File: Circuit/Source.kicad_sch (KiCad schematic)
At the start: 42 parts, among them K1 AGQ200A12, Q1 2N7002, Q2 TIP41C, Q3 TIP42C, U2 DG201, U3 OPA2197xD, U4 OPA2197xD, U5 OPA2197xD

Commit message: Output job, Revision Box and reorganise
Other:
- company: Harry and Yuki - EEE3 Instrumentation -> Harry Hill and Yuki Hoshino
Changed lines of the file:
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@@
 	(title_block
 		(title "Signal Source")
-		(date "2026-03-02")
+		(date "2026-05-02")
 		(rev "1.0")
-		(company "Harry and Yuki - EEE3 Instrumentation")
+		(company "Harry Hill and Yuki Hoshino")
+		(comment 1 "LCR Meter")
 	)
 	(text "Bias range:\n±10V\nGain:\n~6.5"

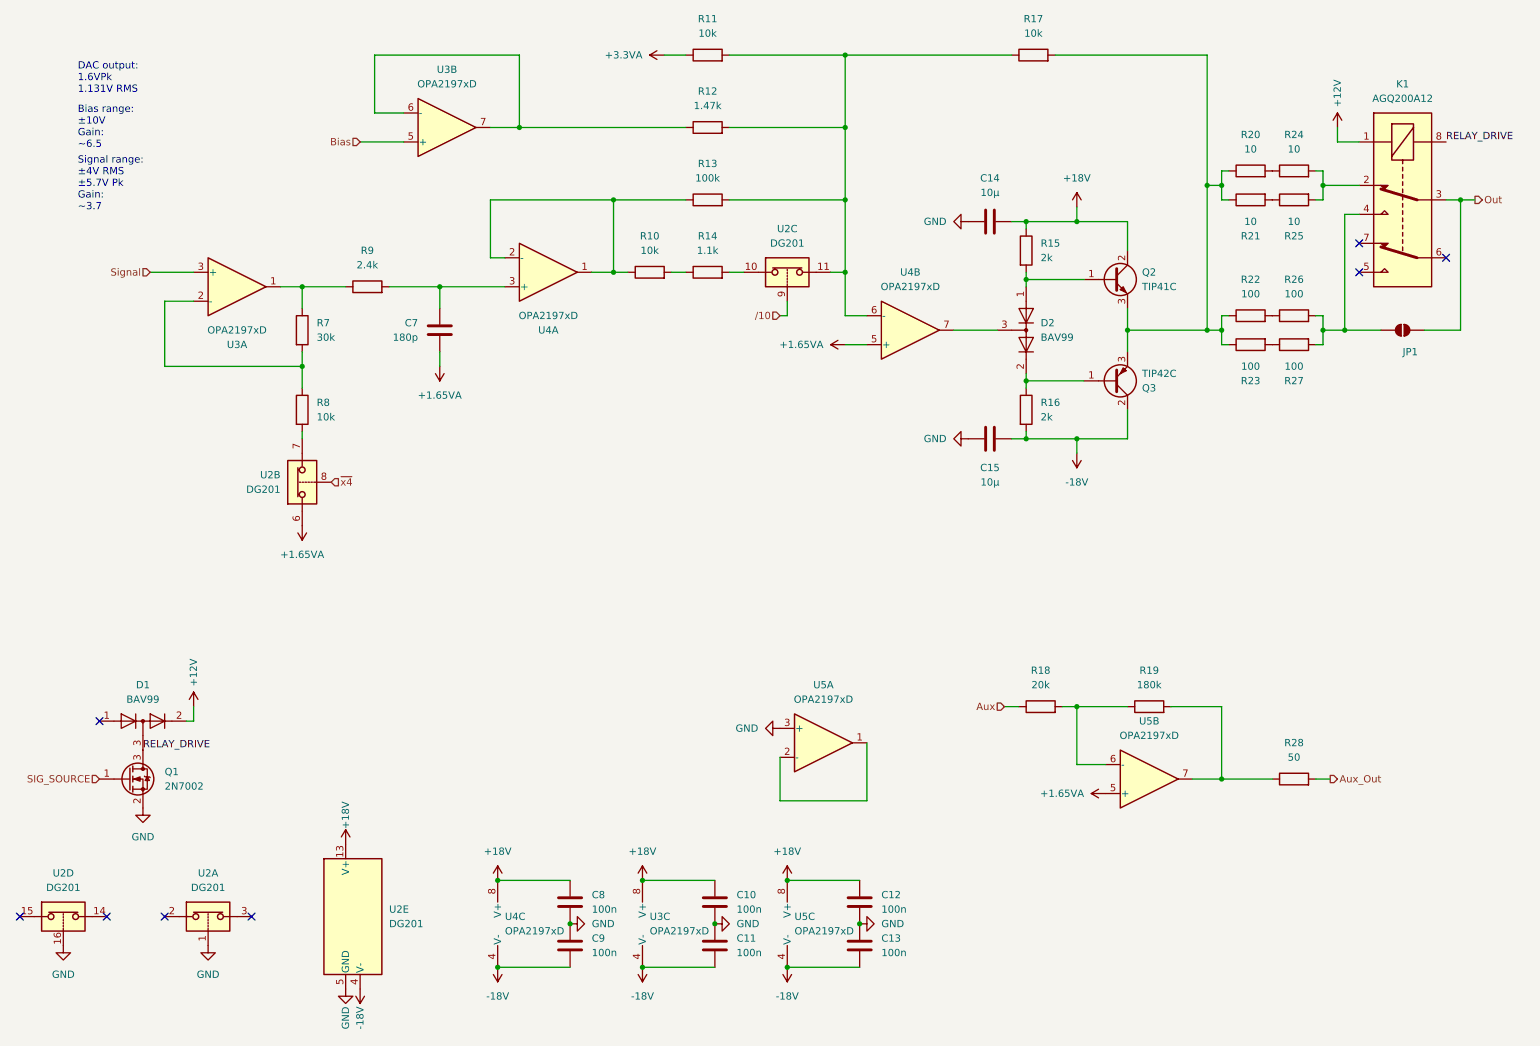
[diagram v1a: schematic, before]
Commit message: Input Protection Second Attempt
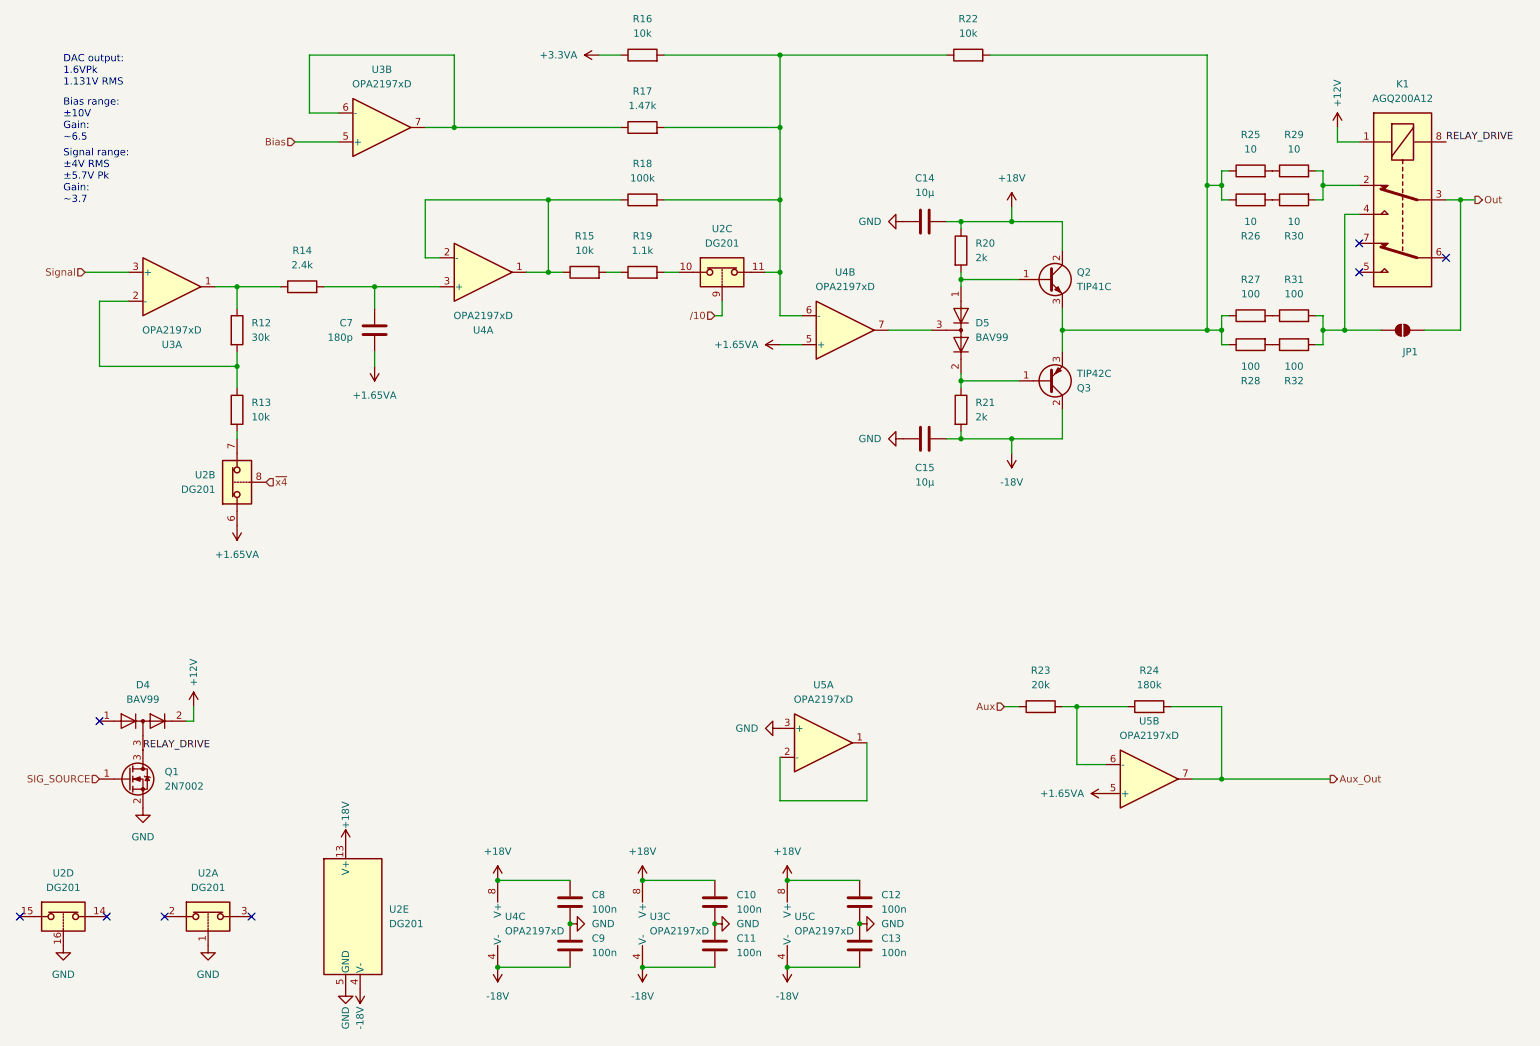
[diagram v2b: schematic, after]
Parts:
- removed R28: 50, Resistor_SMD:R_0805_2012Metric, symbol Device:R
- renumbered D1 to D4, D2 to D5, R7 to R12, R8 to R13, R9 to R14, R10 to R15, R11 to R16, R12 to R17, R13 to R18, R14 to R19, R15 to R20, R16 to R21, R17 to R22, R18 to R23, R19 to R24, R20 to R25, R21 to R26, R22 to R27, R23 to R28, R24 to R29, R25 to R30, R26 to R31, R27 to R32
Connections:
- net Aux_Out: now also R24.2, U5.7
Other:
- moved on the sheet: C14, C15, C7, D5, Q2, Q3, R12, R13, R14, R15, R16, R17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
